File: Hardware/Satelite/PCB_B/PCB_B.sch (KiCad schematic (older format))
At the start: 11 parts, among them IC1 MCP1642B-50I_MS, J1 Conector_PCB_B-C, J2 Conector_PCB_A-B, U1 MIC5323-3.3YD5_TR

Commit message: Nuevo conector B-C
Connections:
- wire segments 127 -> 143
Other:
- moved on the sheet: C3, C4, C5, J1, U1

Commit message: La parte del conector B-C que va en el PCB_B fue movido a bottom mientras que la parte que va en el PCB_C permanece en top
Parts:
- J1: footprint AXTEC:Conector_PCB_B-C -> AXTEC:Conector_PCB_B-C_Lado_B
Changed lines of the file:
@@
 F 0 "J1" H 9050 4567 50  0000 C CNN
 F 1 "Conector_PCB_B-C" H 9050 4475 50  0000 C CNN
-F 2 "AXTEC:Conector_PCB_B-C" H 8950 4600 50  0001 C CNN
+F 2 "AXTEC:Conector_PCB_B-C_Lado_B" H 8950 4600 50  0001 C CNN
 F 3 "" H 8950 4600 50  0001 C CNN
 	1    9050 3850

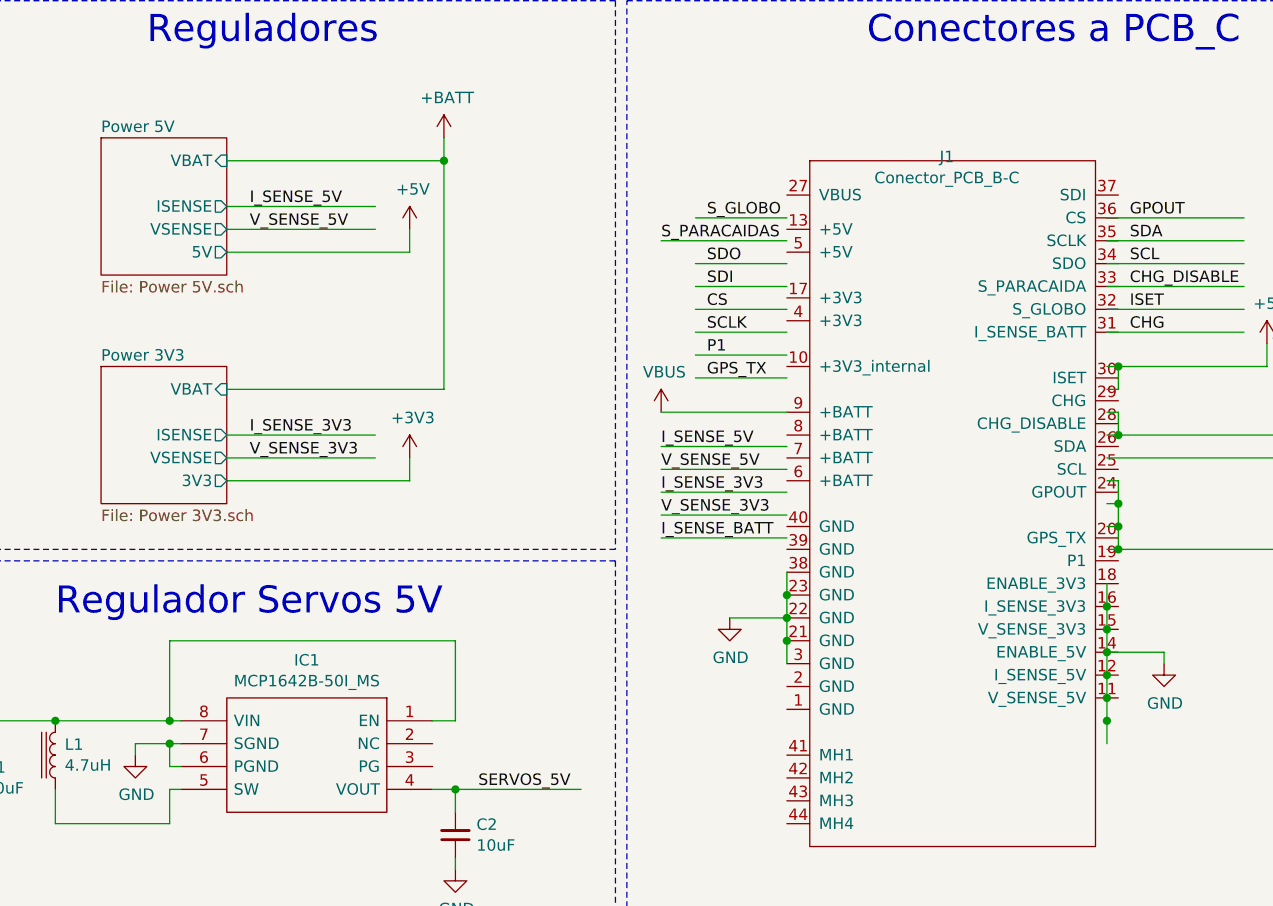
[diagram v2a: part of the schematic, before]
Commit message: Agregado enable de 3v3 y 5v en PCB B. Diseño WIP
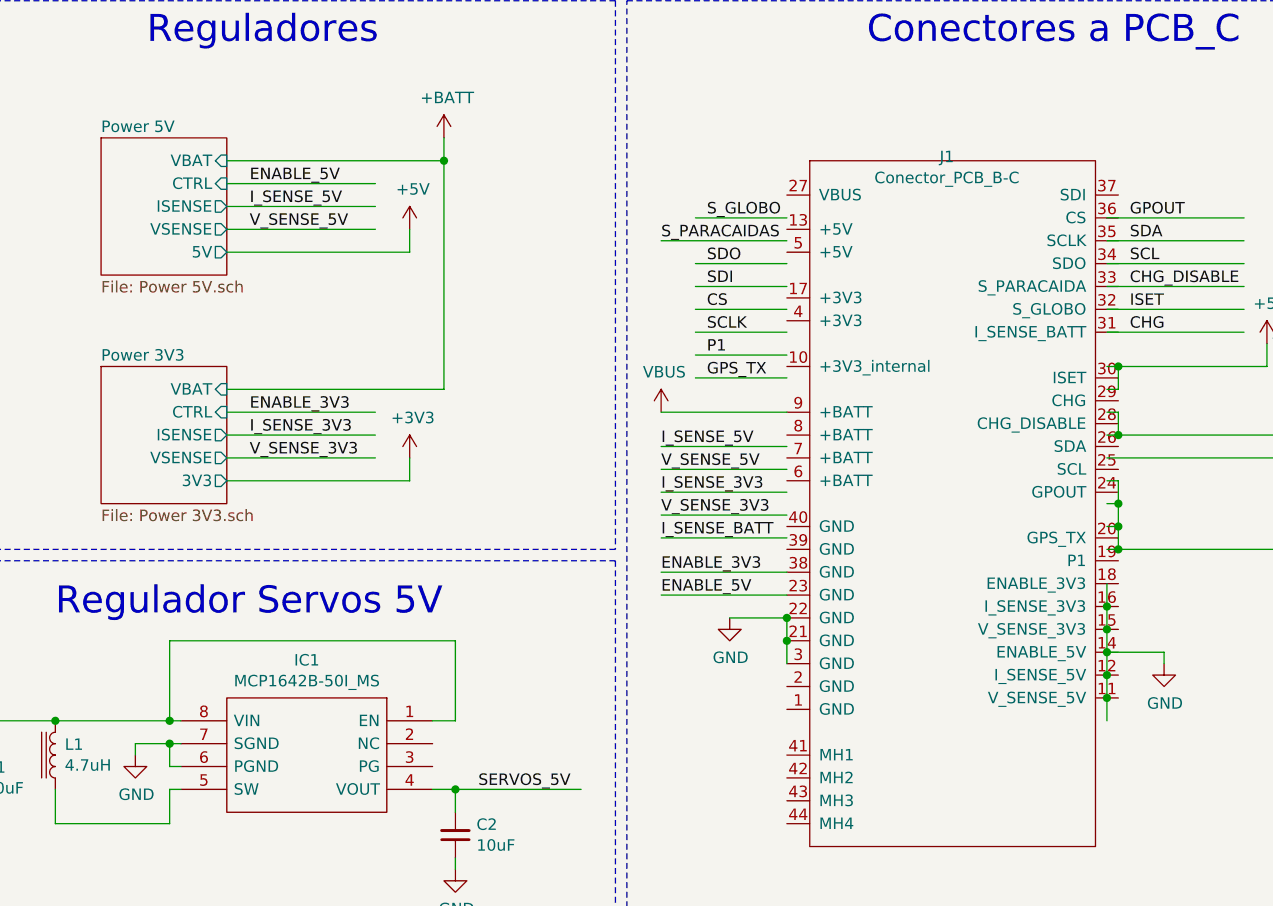
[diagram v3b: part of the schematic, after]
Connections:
- net labels added: ENABLE_3V3, ENABLE_5V
- wire segments 143 -> 144
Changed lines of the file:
@@
 F4 "VSENSE" O R 5900 4450 50
 F5 "3V3" O R 5900 4550 50
+F6 "CTRL" I R 5900 4250 50
 $EndSheet
 $Sheet
@@
 F4 "VSENSE" O R 5900 3450 50
 F5 "5V" O R 5900 3550 50
+F6 "CTRL" I R 5900 3250 50
 $EndSheet
 $Comp
@@
 Text Label 10400 1200 0    50   ~ 0
 P1
-Wire Wire Line
-	9750 5000 9750 5100
-$Comp
-L AXTEC_IC:Conector_PCB_B-C J1
-U 1 1 5BD2AA01
-P 9050 3850
-F 0 "J1" H 9050 4567 50  0000 C CNN
-F 1 "Conector_PCB_B-C" H 9050 4475 50  0000 C CNN
-F 2 "AXTEC:Conector_PCB_B-C_Lado_B" H 8950 4600 50  0001 C CNN
-F 3 "" H 8950 4600 50  0001 C CNN
-	1    9050 3850
-	1    0    0    -1
-$EndComp
 $Comp
 L power:VBUS #PWR0116
@@
 Wire Wire Line
 	9750 4150 9800 4150
-Wire Wire Line
-	9750 5700 9750 5600
-Connection ~ 9750 5100
-Connection ~ 9750 5200
-Wire Wire Line
-	9750 5200 9750 5100
 Connection ~ 9750 5300
 Wire Wire Line
-	9750 5300 9750 5200
-Connection ~ 9750 5400
-Wire Wire Line
-	9750 5400 9750 5300
-Connection ~ 9750 5500
-Wire Wire Line
-	9750 5500 9750 5400
-Connection ~ 9750 5600
-Wire Wire Line
-	9750 5600 9750 5500
-Wire Wire Line
 	10000 5350 10000 5300
 Wire Wire Line
 	10000 5300 9750 5300
 $Comp
-L power:GND #PWR?
+L power:GND #PWR0158
 U 1 1 5BD10C8F
 P 8100 5150
-F 0 "#PWR?" H 8100 4900 50  0001 C CNN
+F 0 "#PWR0158" H 8100 4900 50  0001 C CNN
 F 1 "GND" H 8104 4976 50  0000 C CNN
 F 2 "" H 8100 5150 50  0001 C CNN
@@
 	1    0    0    -1
 $EndComp
+Connection ~ 8350 5150
+Wire Wire Line
+	8350 5150 8100 5150
+Wire Wire Line
+	9750 5600 9750 5500
+Connection ~ 9750 5500
+Wire Wire Line
+	9750 5300 9750 5200
+Connection ~ 9750 5200
+Wire Wire Line
+	9750 5200 9750 5100
+Wire Wire Line
+	9750 5000 9750 5100
+Connection ~ 9750 5100
+Wire Wire Line
+	8350 5250 8350 5150
 Wire Wire Line
 	8350 5350 8350 5250
-Connection ~ 8350 5050
-Wire Wire Line
-	8350 5050 8350 4950
-Connection ~ 8350 5150
-Wire Wire Line
-	8350 5150 8350 5050
 Connection ~ 8350 5250
 Wire Wire Line
-	8350 5250 8350 5150
-Wire Wire Line
-	8350 5150 8100 5150
+	9750 5500 9750 5400
+Wire Wire Line
+	9750 5400 9750 5300
+Connection ~ 9750 5400
+$Comp
+L AXTEC_IC:Conector_PCB_B-C J1
+U 1 1 5BD2AA01
+P 9050 3850
+F 0 "J1" H 9050 4567 50  0000 C CNN
+F 1 "Conector_PCB_B-C" H 9050 4475 50  0000 C CNN
+F 2 "AXTEC:Conector_PCB_B-C_Lado_B" H 8950 4600 50  0001 C CNN
+F 3 "" H 8950 4600 50  0001 C CNN
+	1    9050 3850
+	1    0    0    -1
+$EndComp
+Wire Wire Line
+	5900 3250 6550 3250
+Wire Wire Line
+	5900 4250 6550 4250
+Text Label 6000 4250 0    50   ~ 0
+ENABLE_3V3
+Text Label 6000 3250 0    50   ~ 0
+ENABLE_5V
+Wire Wire Line
+	8350 4950 7800 4950
+Wire Wire Line
+	8350 5050 7800 5050
+Text Label 7800 4950 0    50   ~ 0
+ENABLE_3V3
+Text Label 7800 5050 0    50   ~ 0
+ENABLE_5V
 $EndSCHEMATC

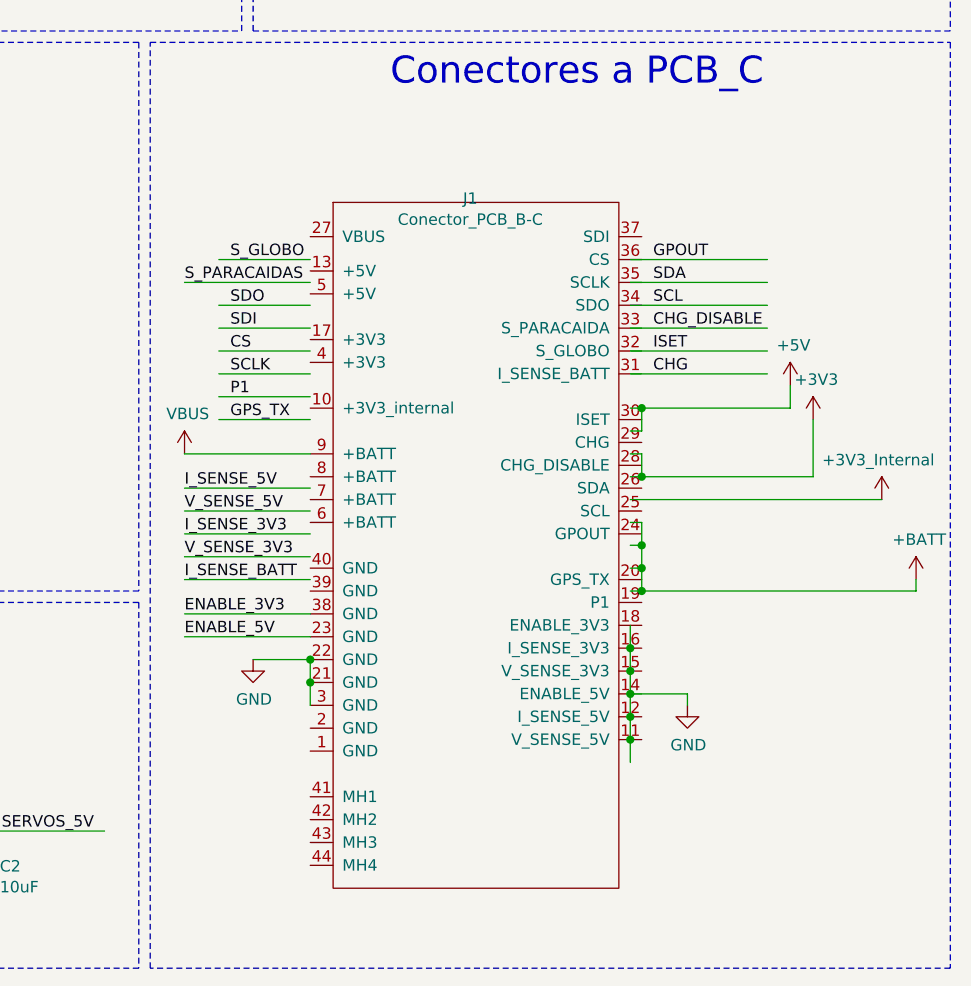
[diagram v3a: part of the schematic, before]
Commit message: Modifificaciones de pines en conector PCB_B-C
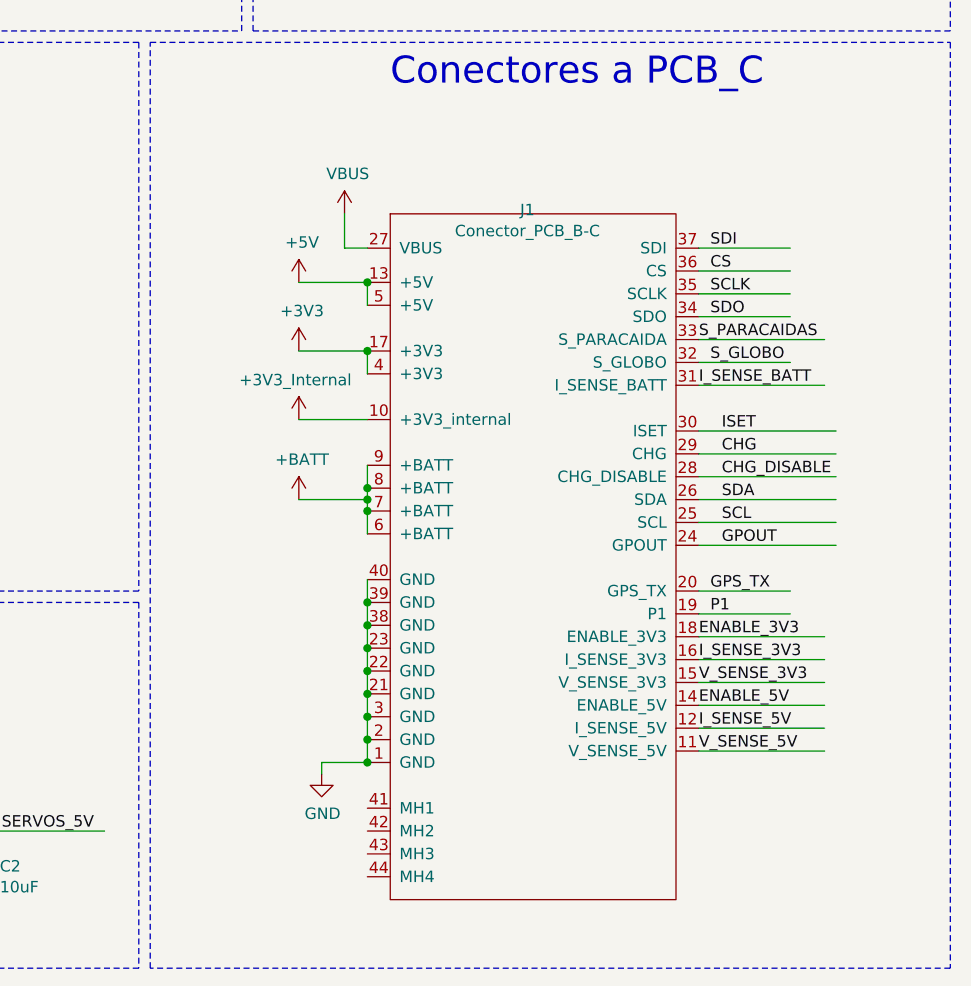
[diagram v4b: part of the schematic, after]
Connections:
- wire segments 144 -> 134
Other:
- moved on the sheet: J1
